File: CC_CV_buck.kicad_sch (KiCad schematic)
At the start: 76 parts, among them J5 Conn_01x02_Pin, J6 Conn_01x02_Pin, J7 Conn_01x02_Pin, J8 Conn_01x02_Pin, Q1 TIP42C, Q2 AO3400A, Q3 MMBT3906, Q4 MMBT3904, U1 OPA2197xD, U2 INA194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

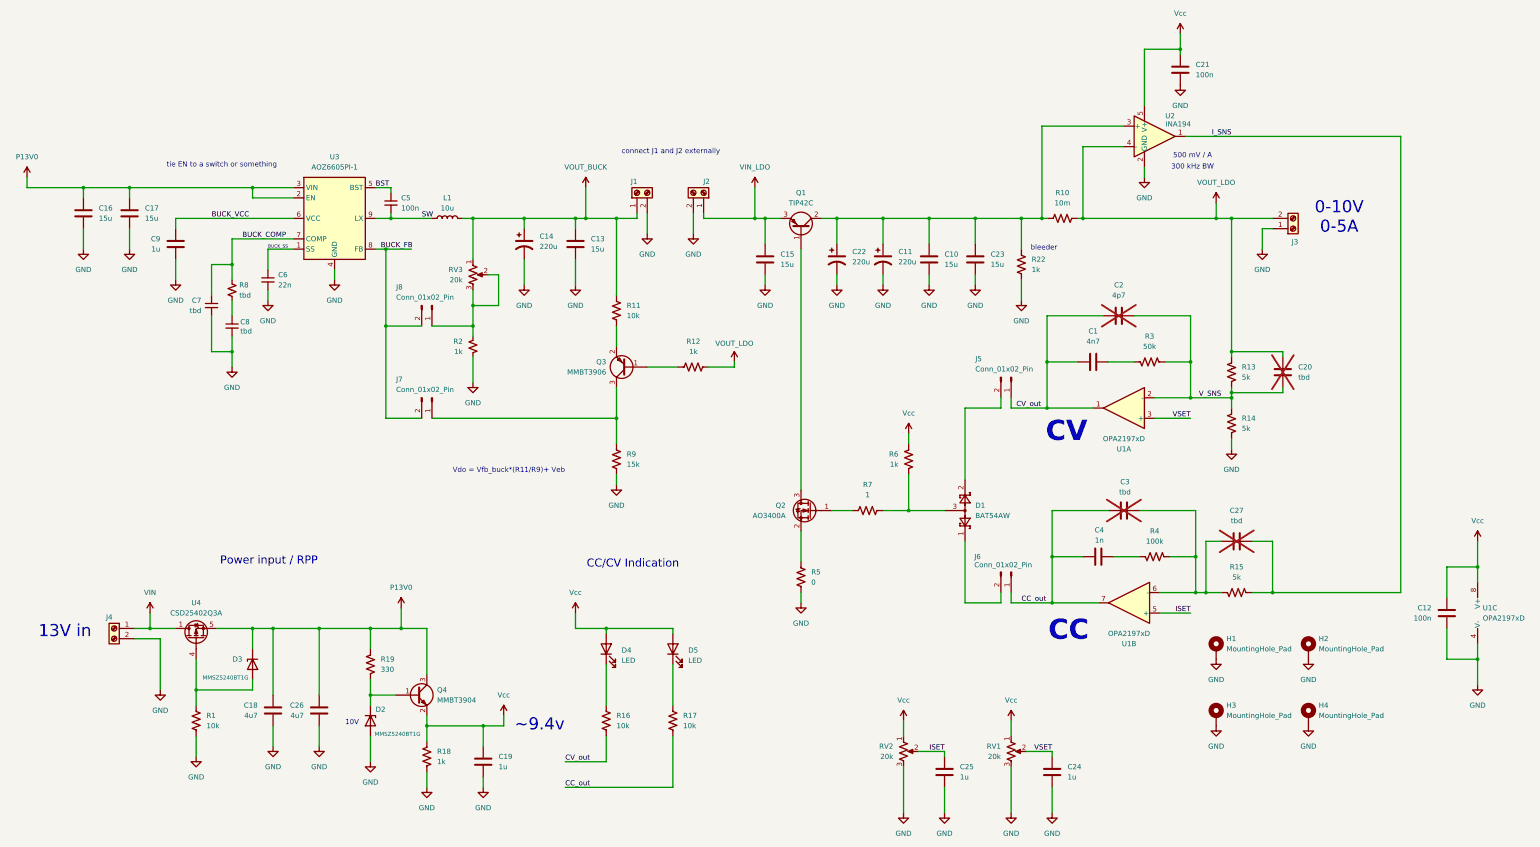
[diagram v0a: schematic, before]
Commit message: change regulator and finish layout
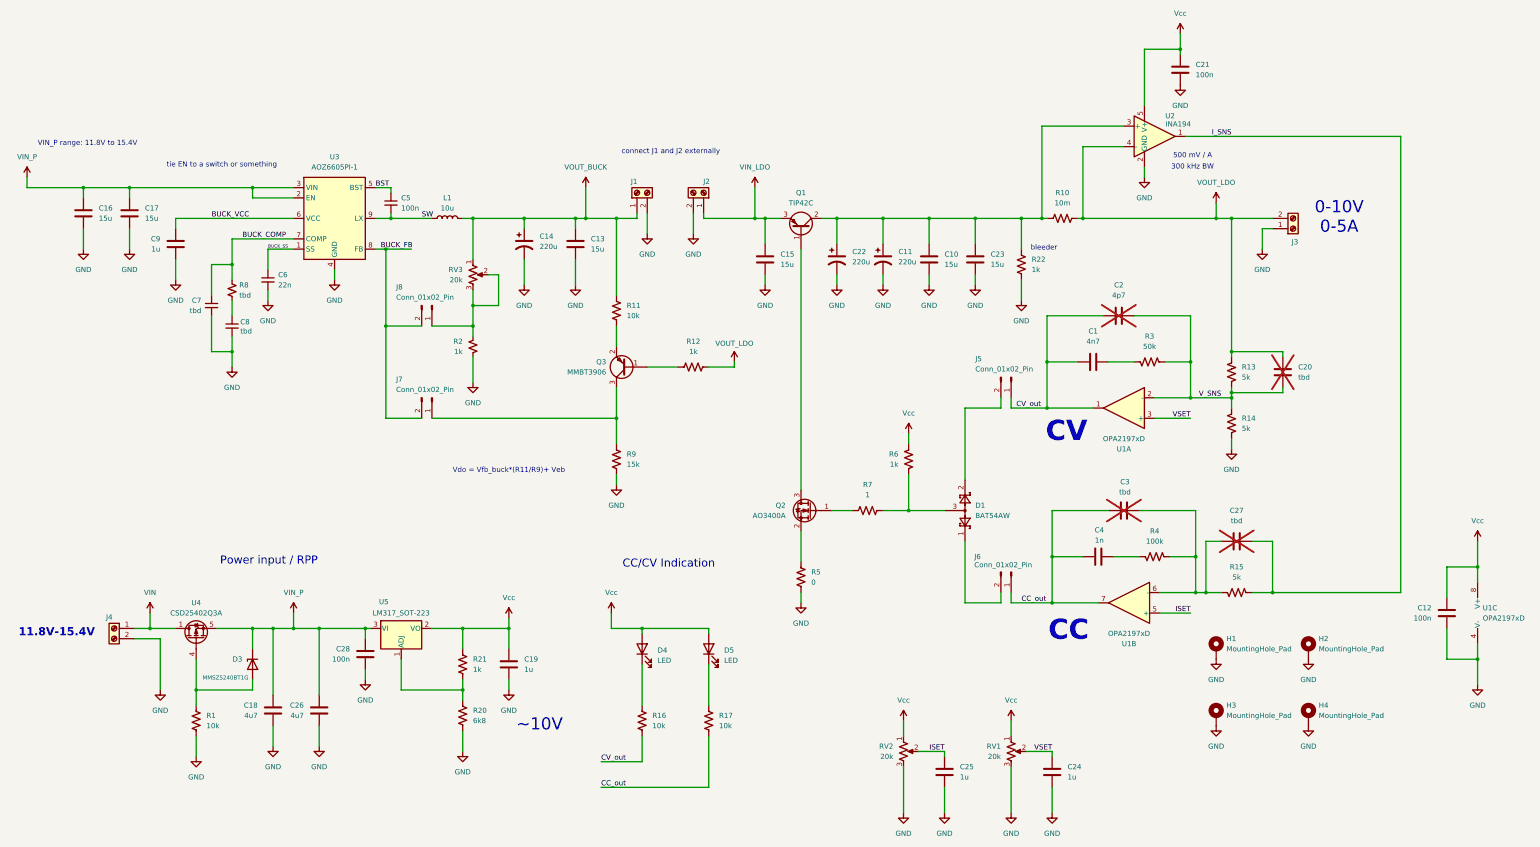
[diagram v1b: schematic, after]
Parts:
- removed D2: MMSZ5240BT1G, Diode_SMD:D_SOD-123, symbol Device:D_Zener
- removed Q4: MMBT3904, Package_TO_SOT_SMD:SOT-23, symbol Transistor_BJT:MMBT3904
- removed R18: 1k, Resistor_SMD:R_0805_2012Metric_Pad1.20x1.40mm_HandSolder, symbol Device:R_US
- removed R19: 330, Resistor_SMD:R_0805_2012Metric_Pad1.20x1.40mm_HandSolder, symbol Device:R_US
- added C28: 100n, Capacitor_SMD:C_0805_2012Metric_Pad1.18x1.45mm_HandSolder, symbol Device:C
- added R20: 6k8, Resistor_SMD:R_0805_2012Metric_Pad1.20x1.40mm_HandSolder, symbol Device:R_US
- added R21: 1k, Resistor_SMD:R_0805_2012Metric_Pad1.20x1.40mm_HandSolder, symbol Device:R_US
- added U5: LM317_SOT-223, Package_TO_SOT_SMD:SOT-223-3_TabPin2, symbol Regulator_Linear:LM317_SOT-223
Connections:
- net GND: now also C28.2, R20.2
- net Vcc: now also R21.1, U5.2 (VO)
- net P13V0 renamed VIN_P
- net VIN_P: now also C28.1, U5.3 (VI)
- new net: R20.1, R21.2, U5.1 (ADJ)
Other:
- note added: "11.8V-15.4V"
- note added: "VIN_P range: 11.8V to 15.4V"
- note added: "~10V"
- note removed: "10V"
- note removed: "13V in"
- note removed: "~9.4v"
- moved on the sheet: C19, D4, D5, R16, R17

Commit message: clean silkscreen and refdes
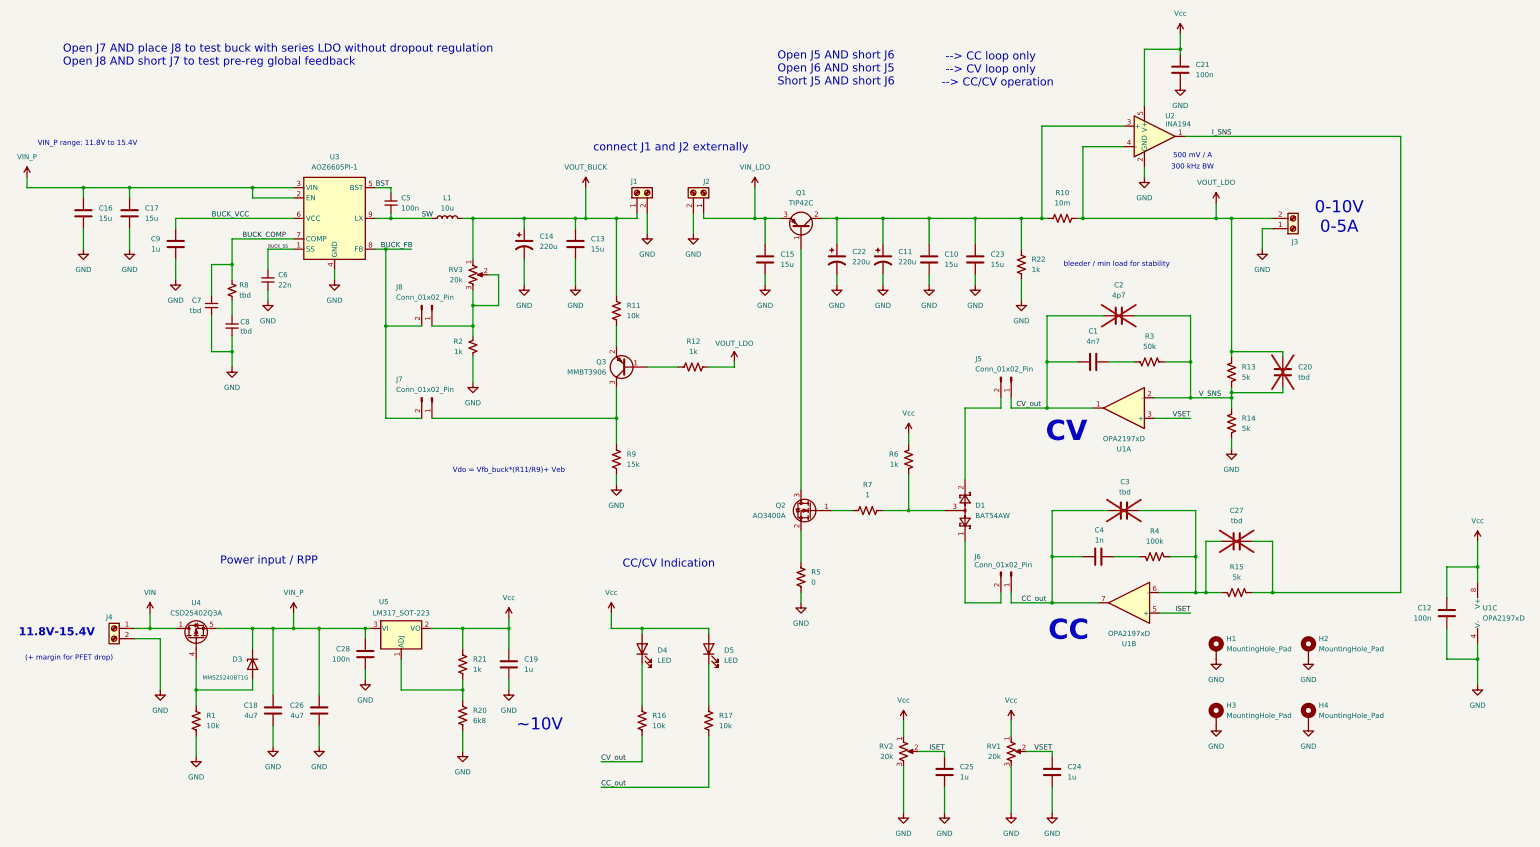
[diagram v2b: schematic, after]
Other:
- note added: "(+ margin for PFET drop)"
- note added: "--> CC loop only --> CV loop only --> CC/CV operation"
- note added: "Open J5 AND short J6 Open J6 AND short J5 Short J5 AND short J6"
- note added: "Open J7 AND place J8 to test buck with series LDO without dropout regulation Open J8 AND short J7 to test pre-reg global feedback"
- note added: "bleeder / min load for stability"
- note removed: "bleeder"
- note removed: "tie EN to a switch or something"
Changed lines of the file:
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@@
+		)
+	)
+	(text "Open J7 AND place J8 to test buck with series LDO without dropout regulation\nOpen J8 AND short J7 to test pre-reg global feedback"
+		(exclude_from_sim no)
+		(at 25.4 32.004 0)
+		(effects
+			(font
+				(size 2 2)
+			)
+			(justify left)
 		)
 	)
@@
 		)
 	)
-	(text "bleeder\n"
+	(text "Open J5 AND short J6  \nOpen J6 AND short J5\nShort J5 AND short J6"
 		(exclude_from_sim no)
-		(at 268.478 79.756 0)
+		(at 202.438 35.306 0)
 		(effects
 			(font
-				(size 1.27 1.27)
+				(size 2 2)
 			)
+			(justify left)
 		)
 	)
-	(text "tie EN to a switch or something "
+	(text "bleeder / min load for stability\n\n"
 		(exclude_from_sim no)
-		(at 64.77 59.182 0)
+		(at 286.512 84.836 0)
 		(effects
 			(font
@@
 		(exclude_from_sim no)
 		(at 305.308 56.896 0)
+		(effects
+			(font
+				(size 1.27 1.27)
+			)
+		)
+	)
+	(text "(+ margin for PFET drop)"
+		(exclude_from_sim no)
+		(at 26.924 181.356 0)
 		(effects
 			(font
@@
 	(text "connect J1 and J2 externally"
 		(exclude_from_sim no)
-		(at 176.022 55.88 0)
+		(at 176.022 54.864 0)
 		(effects
 			(font
-				(size 1.27 1.27)
+				(size 2 2)
 			)
 		)
+	)
+	(text "--> CC loop only\n--> CV loop only\n    --> CC/CV operation"
+		(exclude_from_sim no)
+		(at 255.27 35.56 0)
+		(effects
+			(font
+				(size 2 2)
+			)
+		)

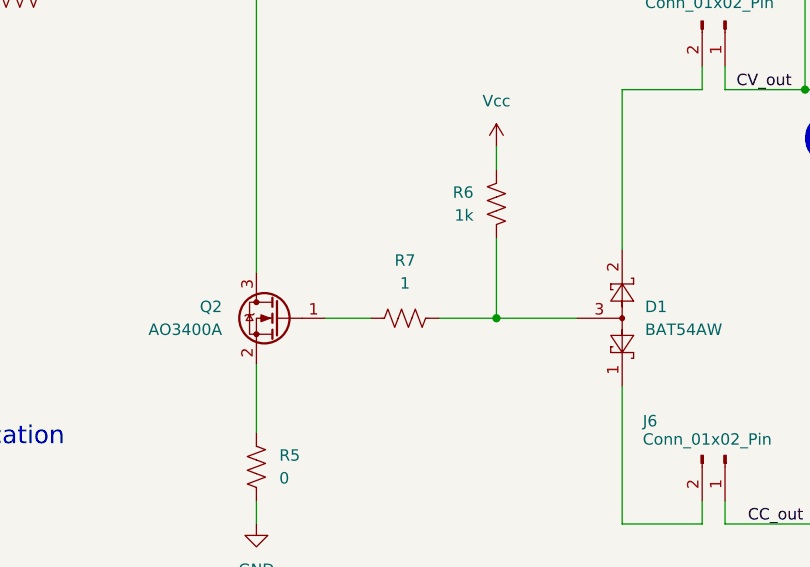
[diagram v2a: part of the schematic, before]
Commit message: change R7 to 0 ohm instead of 1 ohm
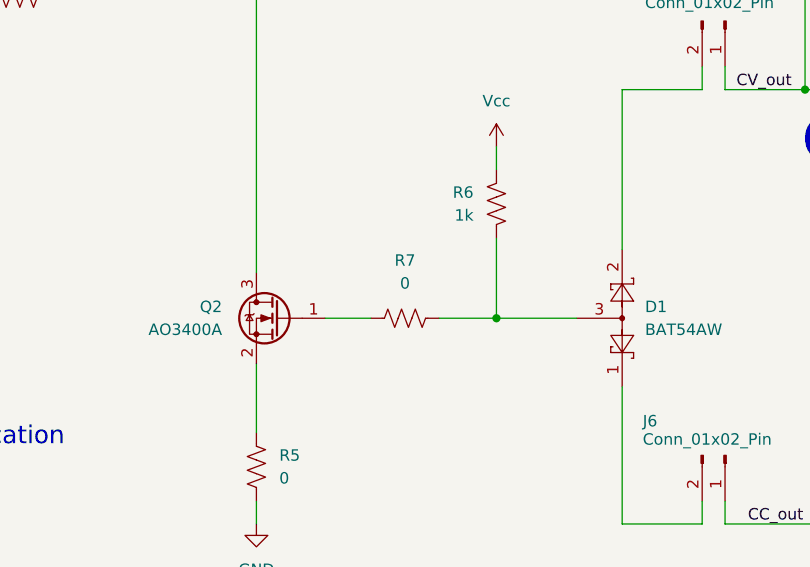
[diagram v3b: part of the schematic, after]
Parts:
- R7: value 1 -> 0
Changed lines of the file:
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@@
 			)
 		)
-		(property "Value" "1"
+		(property "Value" "0"
 			(at 224.79 140.901 90)
 			(effects

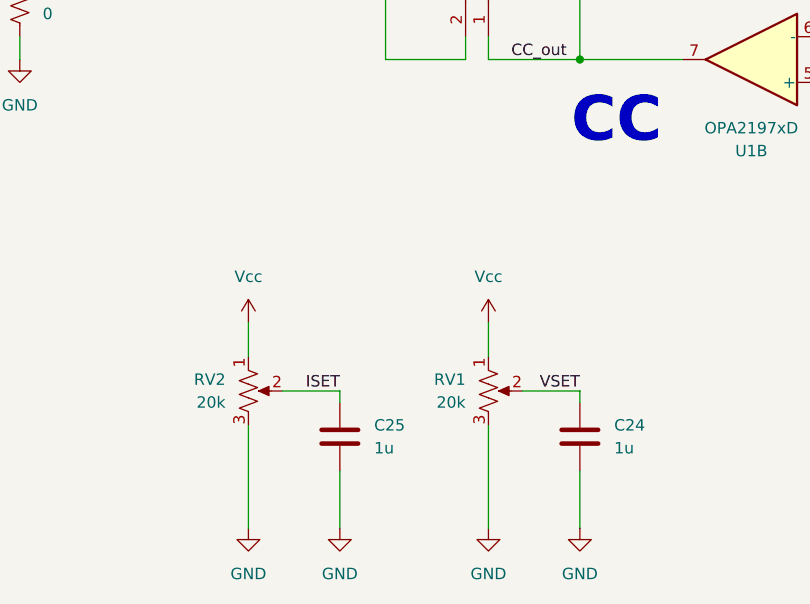
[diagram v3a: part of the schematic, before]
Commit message: for some reason RV1-2 series resistors vanished from schematic, fixed
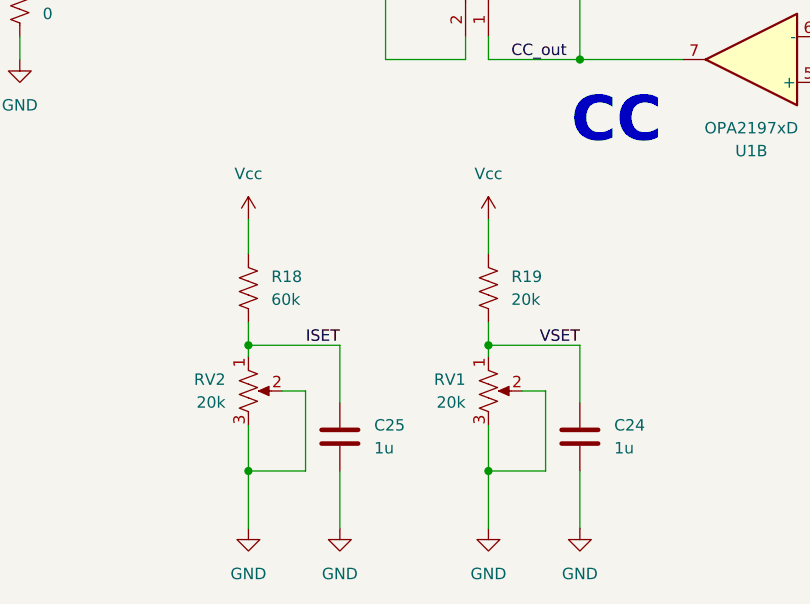
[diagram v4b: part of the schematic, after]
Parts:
- added R18: 60k, Resistor_SMD:R_0805_2012Metric_Pad1.20x1.40mm_HandSolder, symbol Device:R_US
- added R19: 20k, Resistor_SMD:R_0805_2012Metric_Pad1.20x1.40mm_HandSolder, symbol Device:R_US
- J1, J2, J3, J4: footprint TerminalBlock_Phoenix_MPT-0,5-2-2.54_1x02_P2.54mm_Horizontal -> TerminalBlock_Phoenix:TerminalBlock_Phoenix_MPT-0,5-2-2.54_1x02_P2.54mm_Horizontal
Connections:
- net GND: now also RV1.2, RV2.2
- net ISET: now also RV2.1, R18.2; no longer RV2.2
- net VSET: now also RV1.1, R19.2; no longer RV1.2
- net Vcc: now also R18.1, R19.1; no longer RV1.1, RV2.1
